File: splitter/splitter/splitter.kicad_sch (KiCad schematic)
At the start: 33 parts, among them J1 JACKIN, J2 JACKSEND, J3 JACKRECV, J4 JACKOUT, J5 Jack-DC, J6 JACKSEND2, J7 RING_SEND, J8 JACKRECV2, J9 RING_RECV, SW1 SW_MODE, SW2 SW_BYPASS, U1 TL074, U2 TLE2426xLP

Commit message: switch b board
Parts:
- added J10: Conn_01x08, kicad-official/Connector_PinSocket_2.54mm.pretty:PinSocket_2x04_P2.54mm_Vertical, symbol Connector_Generic:Conn_01x08
- added J11: Conn_01x08, kicad-official/Connector_PinHeader_2.54mm.pretty:PinHeader_2x04_P2.54mm_Vertical, symbol Connector_Generic:Conn_01x08
- RV1: symbol splitter-rescue:R_POT_Dual_Separate-Device -> Device:R_Potentiometer_Dual_Separate
- RV2: symbol splitter-rescue:R_POT-Device -> Device:R_Potentiometer
- SW2: footprint Connector_PinSocket_2.54mm:PinSocket_3x03_P2.54mm_Vertical -> _effects_shared_footprints:Stompbox Switch; symbol splitter-rescue:SW_3PDT_x3-Switch -> _effects_shared:SW_3PDT_x3-Switch
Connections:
- net +9V: now also J10.2 (Pin_2); no longer SW2.1 (A)
- net IN: now also J10.5 (Pin_5); no longer SW2.6 (C)
- net OUT: now also J10.3 (Pin_3); no longer SW2.4 (A)
- net DC_IN: now reaches J5.1
- net DC_IN: now also J10.1 (Pin_1); no longer SW2.2 (B)
- net OUTT: now reaches J4.T
- net OUTT: now also J10.8 (Pin_8); no longer SW2.5 (B)
- net RECVR: now reaches JP3.2 (B)
- net RECVR: now also J10.4 (Pin_4); no longer SW2.7 (A)
- net OUTR: now reaches J4.R
- net OUTR: now also J10.6 (Pin_6); no longer SW2.8 (B)
- net INR: now reaches J1.R, JP1.1 (A)
- net INR: now also J10.7 (Pin_7); no longer SW2.9 (C)
- new net 9V_B: J11.2 (Pin_2), SW2.1 (A)
- new net DC_IN_B: J11.1 (Pin_1), SW2.2 (B)
- new net INR_B: J11.7 (Pin_7), SW2.9 (C)
- new net IN_B: J11.5 (Pin_5), SW2.6 (C)
- new net OUTR_B: J11.6 (Pin_6), SW2.8 (B)
- new net OUTT_B: J11.8 (Pin_8), SW2.5 (B)
- new net OUT_B: J11.3 (Pin_3), SW2.4 (A)
- new net RECVR_B: J11.4 (Pin_4), SW2.7 (A)
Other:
- note added: "Bypass switch board interconnect"
- moved on the sheet: J4

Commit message: more adjustments
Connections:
- net DC_IN is gone; now on net +9V: J10.1 (Pin_1), J5.1
- net DC_IN_B is gone; now on net 9V_B: J11.1 (Pin_1), SW2.2 (B)
- net +9V: no longer D1.2 (A), J10.2 (Pin_2)
- net 9V_B: no longer J11.2 (Pin_2), SW2.1 (A)
- new net LED: D1.2 (A), J10.2 (Pin_2)
- new net LED_B: J11.2 (Pin_2), SW2.1 (A)
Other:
- moved on the sheet: J5, SW2A

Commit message: cleanup
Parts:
- removed J7: RING_SEND, Connector_PinSocket_2.54mm:PinSocket_1x02_P2.54mm_Vertical, symbol Connector:Conn_01x02_Female
- removed J9: RING_RECV, Connector_PinSocket_2.54mm:PinSocket_1x02_P2.54mm_Vertical, symbol Connector:Conn_01x02_Female
- removed JP1: JMP_RING_SEND, Jumper:SolderJumper-2_P1.3mm_Open_RoundedPad1.0x1.5mm, symbol Jumper:Jumper_2_Bridged
- removed JP3: JMP_RING_RECV, Jumper:SolderJumper-2_P1.3mm_Open_RoundedPad1.0x1.5mm, symbol Jumper:Jumper_2_Bridged
- added JP2: STEREO_MODE, symbol Jumper:SolderJumper_3_Open
- added JP3: STEREO_MODE_RETURN, symbol Jumper:SolderJumper_3_Open
- added R? (x2): 100K, Resistor_THT:R_Axial_DIN0207_L6.3mm_D2.5mm_P7.62mm_Horizontal, symbol Device:R
- R7, R8: value 470K -> 100K
- R9: value 1M -> 1.2M
- RV2: value B1M_MIX -> B10K_MIX
- renumbered JP2 to JP1
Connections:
- net GND: now also RV2.2; no longer SW1.6
- net IN: now also R4.1; no longer R4.2, SW1.2
- net INR: now also JP2.1 (A)
- net RECVR: now also JP3.1 (A)
- net at R9.1, U1.9 (-): now also R?.2, R?.2; no longer RV2.2
- net HALF_IN: now reaches R5.2, U1.12 (+)
- net HALF_IN: now also R4.2, SW1.2, SW1.6; no longer R4.1
- net at R8.1, RV2.1: now also R?.1
- net at R7.2, RV2.3: now also R?.1
- net at J3.R: now also JP3.2 (C)
- net at J2.R, J3.RN: now also JP2.2 (C)
- net RECV_DRY renamed RECV_2
- net RECV_2: now also JP3.3 (B)
- net RECV_WET renamed RECV_1
- net SEND_DRY renamed SEND_2
- net SEND_2: now also JP2.3 (B)
- net SEND_WET renamed SEND_1
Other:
- note added: "Optional, if you want two send-receive channels. If not, tie the jumper closed and leave the jacks unpopulated"
- note added: "Stereo jumpers control the behavior of the ring channel (if stereo cables are used). 2-1: true bypass of signal on or off, no effect 2-3: dry signal on send/receive ring channel"
- note added: "input impedance: >=100K op-amp output impedance (20mA @ 0.5V?)"
- note removed: "Optional, if you want two send-receive channels. If not, tie the jumper closed and leave the jacks off"
- note removed: "input impedance: 470K to 1.4M op-amp output impedance (20mA @ 0.5V?)"
- moved on the sheet: C1, C2, J1, J2, J3, J4, R1, R2, R3, R4, R5, R6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

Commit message: rev D
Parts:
- added C10, C5, C6, C7, C8, C9: 100n, kicad-official/Capacitor_THT.pretty:C_Rect_L7.0mm_W2.5mm_P5.00mm, symbol Device:C
- C1, C2: footprint Capacitor_THT:C_Disc_D4.3mm_W1.9mm_P5.00mm -> kicad-official/Capacitor_THT.pretty:C_Disc_D4.3mm_W1.9mm_P5.00mm
- C3, C4: footprint Capacitor_THT:C_Rect_L7.0mm_W2.0mm_P5.00mm -> kicad-official/Capacitor_THT.pretty:CP_Radial_D5.0mm_P2.50mm
- D1: footprint LED_THT:LED_D3.0mm -> kicad-official/LED_THT.pretty:LED_D3.0mm
- J5: footprint Connector_PinSocket_2.54mm:PinSocket_1x02_P2.54mm_Vertical -> kicad-official/Connector_PinSocket_2.54mm.pretty:PinSocket_1x02_P2.54mm_Vertical
- JP1: footprint Jumper:SolderJumper-2_P1.3mm_Open_RoundedPad1.0x1.5mm -> kicad-official/Jumper.pretty:SolderJumper-2_P1.3mm_Open_RoundedPad1.0x1.5mm
- JP2, JP3: footprint (none) -> kicad-official/Jumper.pretty:SolderJumper-3_P1.3mm_Open_RoundedPad1.0x1.5mm
- R1, R10, R2, R3, R4, R5, R6, R7, R8, R9: footprint Resistor_THT:R_Axial_DIN0207_L6.3mm_D2.5mm_P7.62mm_Horizontal -> kicad-official/Resistor_THT.pretty:R_Axial_DIN0207_L6.3mm_D2.5mm_P7.62mm_Horizontal
- R11, R12: renamed from R?; footprint Resistor_THT:R_Axial_DIN0207_L6.3mm_D2.5mm_P7.62mm_Horizontal -> kicad-official/Resistor_THT.pretty:R_Axial_DIN0207_L6.3mm_D2.5mm_P7.62mm_Horizontal
- RV1: footprint Potentiometer_THT:Potentiometer_Alpha_RD902F-40-00D_Dual_Vertical -> kicad-official/Potentiometer_THT.pretty:Potentiometer_Alpha_RD902F-40-00D_Dual_Vertical
- RV2: footprint Potentiometer_THT:Potentiometer_Alpha_RD901F-40-00D_Single_Vertical -> kicad-official/Potentiometer_THT.pretty:Potentiometer_Alpha_RD901F-40-00D_Single_Vertical
- U1: footprint Package_DIP:DIP-14_W7.62mm -> kicad-official/Package_DIP.pretty:DIP-14_W7.62mm_Socket
- U2: footprint Package_TO_SOT_THT:TO-92_Inline_Wide -> kicad-official/Package_TO_SOT_THT.pretty:TO-92_Inline_Wide
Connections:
- net GND: no longer J1.S, J1.SN, J2.S, J2.SN, J3.S, J3.SN, J4.S, J4.SN, J6.S, J6.SN, J8.S, J8.SN
- net GNDD: now also J1.S, J1.SN, J2.S, J2.SN, J3.S, J3.SN, J4.S, J4.SN, J6.S, J6.SN, J8.S, J8.SN
- net IN: now also C5.2; no longer U1.5 (+)
- net OUT: now also C10.2; no longer R9.2, U1.8
- net RECV_1: now also C8.1; no longer R7.1
- net RECV_2: now also C9.2; no longer R8.2
- net SEND_1: now also C6.2; no longer SW1.3
- net SEND_2: now also C7.1; no longer SW1.7
- new net: C5.1, U1.5 (+)
- new net: C10.1, R9.2, U1.8
- new net: C9.1, R8.2
- new net: C8.2, R7.1
- new net: C6.1, SW1.3
- new net: C7.2, SW1.7
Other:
- note added: "22n, 1K -> 7.2z, Q=0.5 22n, 1001K -> 7.2KHz, Q=0.5 Note: subtracting instead of creating separate LP and HP filters creates an uneven split as opposed to summing LR filters. Creating a true crossover would require VCFs, which would be more complicated. DC blocking caps on analog boundaries because of difference in ground reference."
- note added: "Even though our analog reference is 4.5V, other pedals will use the power supply ground (0V) as their ground. So we need to use GNDD for the jack grounds"
- note removed: "22n, 1K -> 7.2z, Q=0.5 22n, 1001K -> 7.2KHz, Q=0.5 Note: subtracting instead of creating separate LP and HP filters creates an uneven split as opposed to summing LR filters. Creating a true crossover would require VCFs, which would be more complicated."
- moved on the sheet: J1, J10, J11, J2, J3, J4, J6, J8, JP1, JP2, JP3, R11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

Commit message: mechanicals and measurements
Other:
- note added: "TODO: consider 1k 6.8n -> 23kHz 1M 6.8n -> 23Hz use 100k sweep, with 10x adjustment to focus measure actual values on good bass settings"
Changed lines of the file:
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@@
+    (effects (font (size 1.27 1.27)) (justify left bottom))
+  )
+  (text "TODO: consider 1k 6.8n -> 23kHz  1M 6.8n -> 23Hz\nuse 100k sweep, with 10x adjustment to focus\nmeasure actual values on good bass settings"
+    (at 89.535 89.535 0)
     (effects (font (size 1.27 1.27)) (justify left bottom))
   )

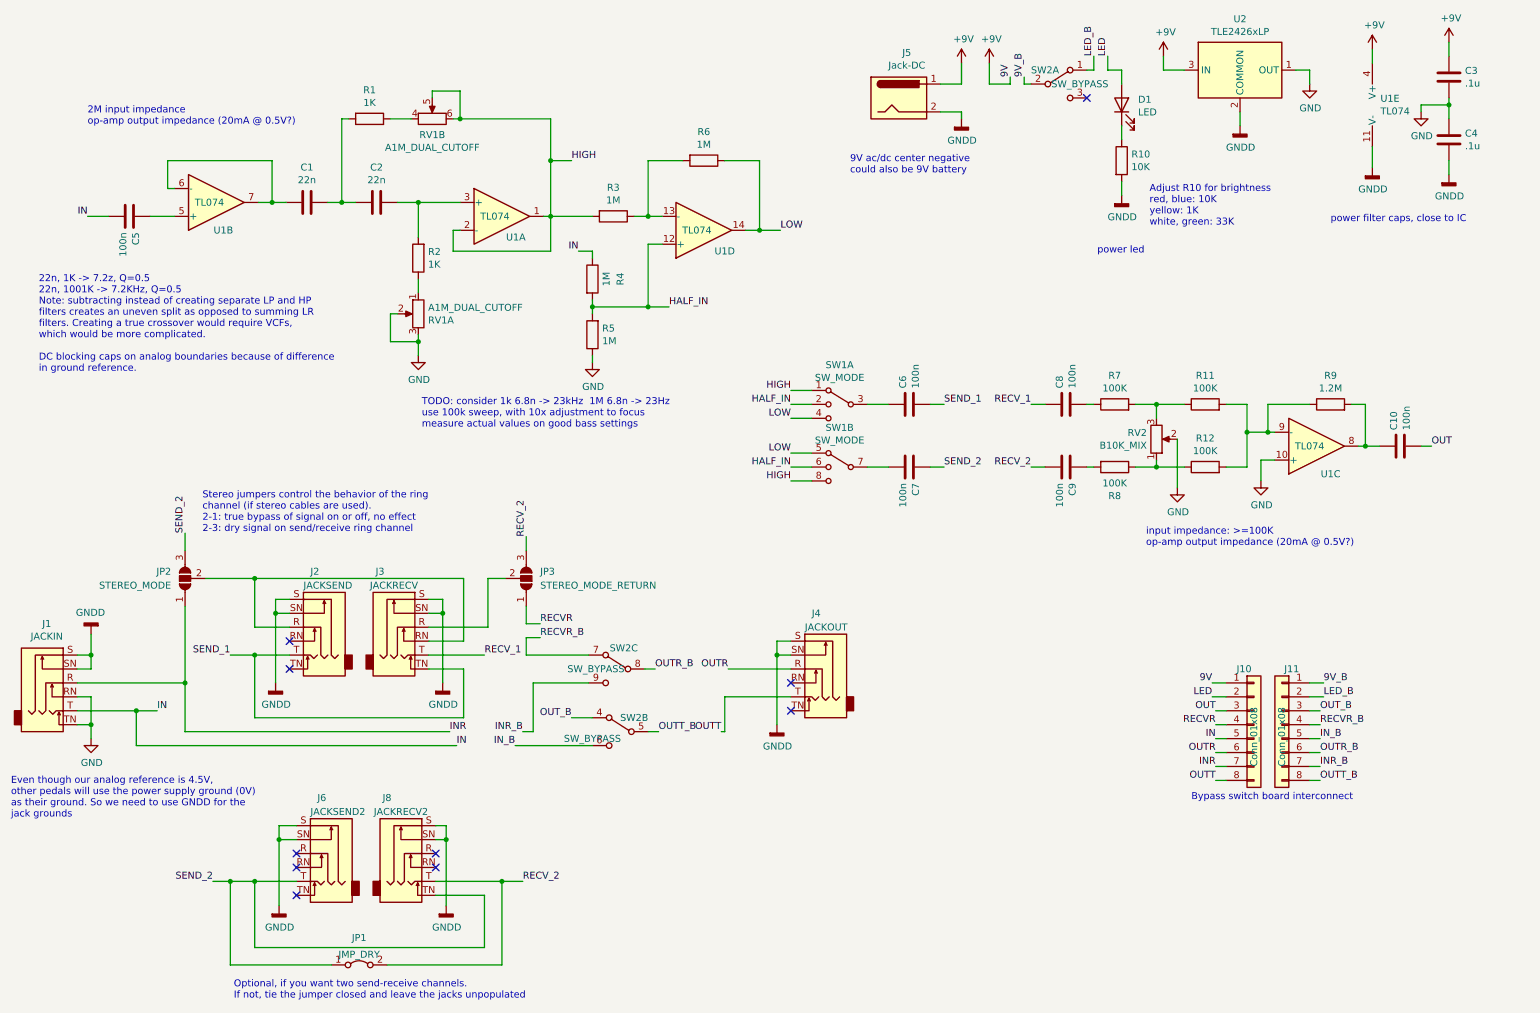
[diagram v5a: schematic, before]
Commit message: fix some spacing, start on graphics
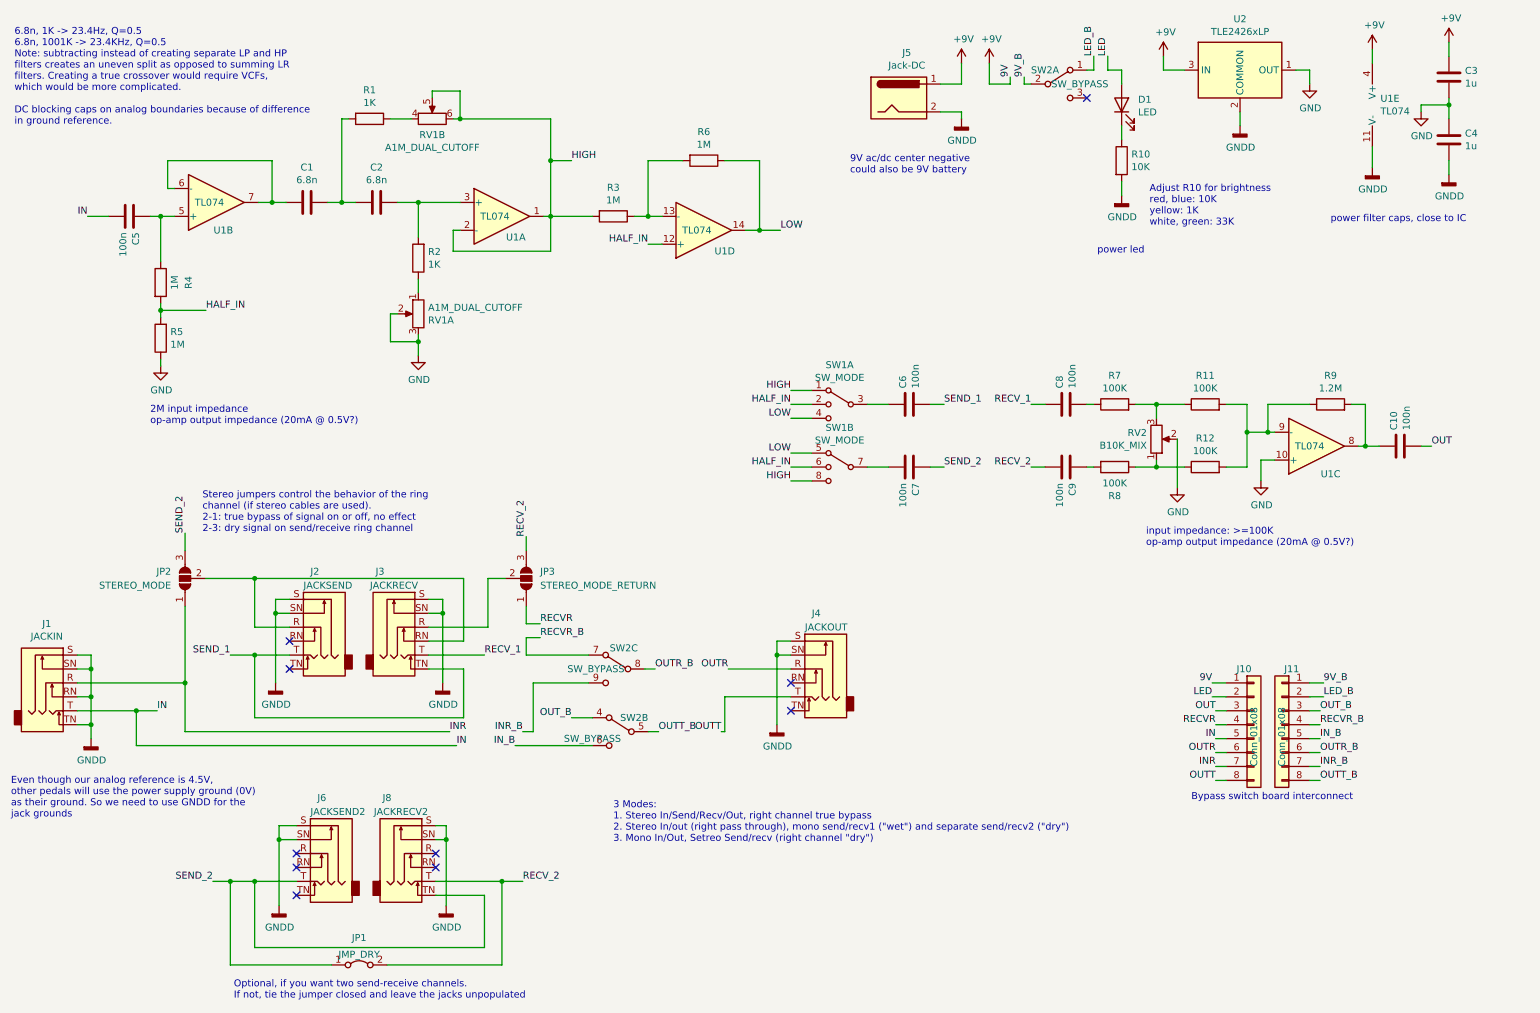
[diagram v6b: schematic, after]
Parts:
- C1, C2: value 22n -> 6.8n; footprint kicad-official/Capacitor_THT.pretty:C_Disc_D4.3mm_W1.9mm_P5.00mm -> kicad-official/Capacitor_THT.pretty:C_Rect_L7.0mm_W2.5mm_P5.00mm
- C3, C4: value .1u -> 1u
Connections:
- net GND: no longer J1.RN, J1.TN
- net GNDD: now also J1.RN, J1.TN
- net IN: no longer R4.1
- net at C5.1, U1.5 (+): now also R4.1
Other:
- note added: "3 Modes: 1. Stereo In/Send/Recv/Out, right channel true bypass 2. Stereo In/out (right pass through), mono send/recv1 ("wet") and separate send/recv2 ("dry") 3. Mono In/Out, Setreo Send/recv (right channel "dry")"
- note added: "6.8n, 1K -> 23.4Hz, Q=0.5 6.8n, 1001K -> 23.4KHz, Q=0.5 Note: subtracting instead of creating separate LP and HP filters creates an uneven split as opposed to summing LR filters. Creating a true crossover would require VCFs, which would be more complicated. DC blocking caps on analog boundaries because of difference in ground reference."
- note removed: "22n, 1K -> 7.2z, Q=0.5 22n, 1001K -> 7.2KHz, Q=0.5 Note: subtracting instead of creating separate LP and HP filters creates an uneven split as opposed to summing LR filters. Creating a true crossover would require VCFs, which would be more complicated. DC blocking caps on analog boundaries because of difference in ground reference."
- note removed: "TODO: consider 1k 6.8n -> 23kHz 1M 6.8n -> 23Hz use 100k sweep, with 10x adjustment to focus measure actual values on good bass settings"
- moved on the sheet: R4, R5

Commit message: rev e
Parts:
- removed R4, R5: 1M, kicad-official/Resistor_THT.pretty:R_Axial_DIN0207_L6.3mm_D2.5mm_P7.62mm_Horizontal, symbol Device:R
- renumbered C5 to C1, C4 to C10, C1 to C2, C2 to C3, C7 to C4, C6 to C5, C8 to C6, C9 to C7, C10 to C8, C3 to C9, J6 to J3, J3 to J4, J8 to J5, J4 to J6, J5 to J7, J10 to J8, J11 to J9, JP2 to JP1, JP1 to JP2, R9 to R10, R6 to R4, R7 to R5, R8 to R6, R10 to R7, R11 to R8, R12 to R9, SW2 to SW1, SW1 to SW2
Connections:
- net HIGH: now also C4.2; no longer R3.2, RV1.5, RV1.6, U1.1, U1.2 (-)
- net IN: now also SW2.2, SW2.6
- net LOW: now also C5.2; no longer R4.1, U1.14
- net SEND_1: now also SW2.3; no longer C5.2
- net SEND_2: now also SW2.7; no longer C4.1
- net at C1.1, U1.5 (+): now also U1.12 (+)
- net at C5.1: now also R4.1, U1.14; no longer SW2.3
- removed net HALF_IN: SW2.2, SW2.6, U1.12 (+)
- new net: C4.1, R3.2, RV1.5, RV1.6, U1.1, U1.2 (-)
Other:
- note added: "Adjust R7 for brightness red, blue: 10K yellow: 1K white, green: 33K"
- note added: "Modes: Mono in/out/send/recv: all jumpers open Stereo in/send/recv/out, right channel switched but not filtered: JP1=closed, JP2+JP3=1:2 Stereo in/out (right pass through), mono send/recv1 ("wet") and separate send/recv2 ("dry"): JP1=open, JP2+JP3=1:2, send2+recv2 jacks populated Mono in/out, stereo send/recv (right channel "dry"): JP1=closed, JP2+JP3=2:3"
- note added: "Stereo jumpers control the behavior of the ring channel (if stereo cables are used). 1::2 - true bypass of signal on or off, no effect 2::3 - dry signal on send/receive ring channel"
- note added: "op-amp input impedance (>1Mohm) op-amp output impedance (20mA @ 0.5V?)"
- note removed: "2M input impedance op-amp output impedance (20mA @ 0.5V?)"
- note removed: "3 Modes: 1. Stereo In/Send/Recv/Out, right channel true bypass 2. Stereo In/out (right pass through), mono send/recv1 ("wet") and separate send/recv2 ("dry") 3. Mono In/Out, Setreo Send/recv (right channel "dry")"
- note removed: "Adjust R10 for brightness red, blue: 10K yellow: 1K white, green: 33K"
- note removed: "Stereo jumpers control the behavior of the ring channel (if stereo cables are used). 2-1: true bypass of signal on or off, no effect 2-3: dry signal on send/receive ring channel"
- moved on the sheet: C4, C5, C6, C7, C8, J6, JP3, R10, R3, R4, R5, R6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

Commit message: update capacitor footprints
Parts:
- C10, C9: footprint kicad-official/Capacitor_THT.pretty:CP_Radial_D5.0mm_P2.50mm -> kicad-official/Capacitor_THT.pretty:CP_Radial_D4.0mm_P1.50mm
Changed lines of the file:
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@@
       (effects (font (size 1.27 1.27)) (justify left))
     )
-    (property "Footprint" "kicad-official/Capacitor_THT.pretty:CP_Radial_D5.0mm_P2.50mm" (id 2) (at 277.8252 29.21 0)
+    (property "Footprint" "kicad-official/Capacitor_THT.pretty:CP_Radial_D4.0mm_P1.50mm" (id 2) (at 277.8252 29.21 0)
       (effects (font (size 1.27 1.27)) hide)
     )
@@
       (effects (font (size 1.27 1.27)) (justify left))
     )
-    (property "Footprint" "kicad-official/Capacitor_THT.pretty:CP_Radial_D5.0mm_P2.50mm" (id 2) (at 277.8252 40.64 0)
+    (property "Footprint" "kicad-official/Capacitor_THT.pretty:CP_Radial_D4.0mm_P1.50mm" (id 2) (at 277.8252 40.64 0)
       (effects (font (size 1.27 1.27)) hide)
     )
@@
     )
     (path "/00000000-0000-0000-0000-0000630a3eff"
-      (reference "C9") (unit 1) (value "1u") (footprint "kicad-official/Capacitor_THT.pretty:CP_Radial_D5.0mm_P2.50mm")
+      (reference "C9") (unit 1) (value "1u") (footprint "kicad-official/Capacitor_THT.pretty:CP_Radial_D4.0mm_P1.50mm")
     )
     (path "/00000000-0000-0000-0000-0000630a4536"
-      (reference "C10") (unit 1) (value "1u") (footprint "kicad-official/Capacitor_THT.pretty:CP_Radial_D5.0mm_P2.50mm")
+      (reference "C10") (unit 1) (value "1u") (footprint "kicad-official/Capacitor_THT.pretty:CP_Radial_D4.0mm_P1.50mm")
     )
     (path "/00000000-0000-0000-0000-0000630c8c10"
